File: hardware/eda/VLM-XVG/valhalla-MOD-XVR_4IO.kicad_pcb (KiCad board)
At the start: 2 copper layers, 206.2 x 99.6 mm, 126 parts, among them J1 POWER, J10 FIM_I, J11 FIM_I, J12 FIM_I, J13 FIM_I, J14 GLM_F, J15 GLM_F, J16 GLM_F, J17 GLM_F, J18 GLM_B, J19 GLM_B, J2 FIELD, J20 GLM_B, J21 GLM_B, J22 WDM_I, J23 WDM_I, J24 TM, J29 WDM_I, J3 GPIO, J31 TM_0, J32 TM_1, J34 WDM_E, J35 WDM_E, J36 WDM_E, J4 FIM_E, J5 FIM_E, J6 FIM_E, J7 FIM_E, J8 FIM_E, J9 FIM_I, Q1 IRLZ44N, Q2 IRLZ44N, Q3 2N3904, Q4 2N3904, Q5 2N3906, Q6 2N3906, U1 4N35, U2 4N35, U3 74HC14, U4 4N35, U5 4N35, U6 74HC74, U8 74HC123, U9 74HC04

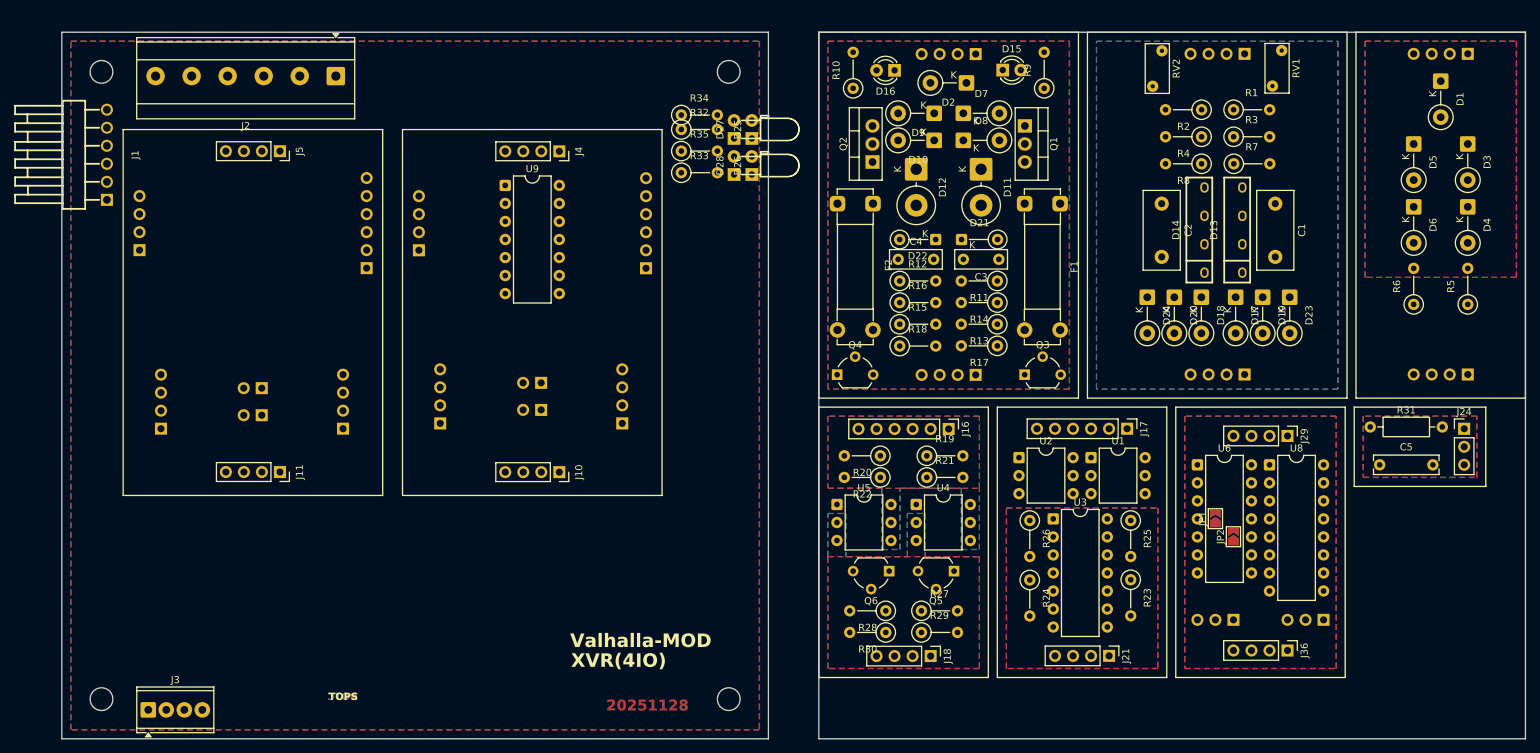
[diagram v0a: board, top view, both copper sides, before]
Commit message: UPDATE: 1st routing pass done on MOD-XVR(4IO)
 - netclass will have to be re-checked on GPI-Mains
   - clearance/creepage values between the two GPI lines
 - netclass will have to be re-checked on GPO-Power
   - ampacity of entire high-power loop
 - polarization for the field interface modules to be added
   - GPIO line modules are already polarized
   - watchdog/debouncer modules are idempotent
 - silkscreen and mechanical details are last.
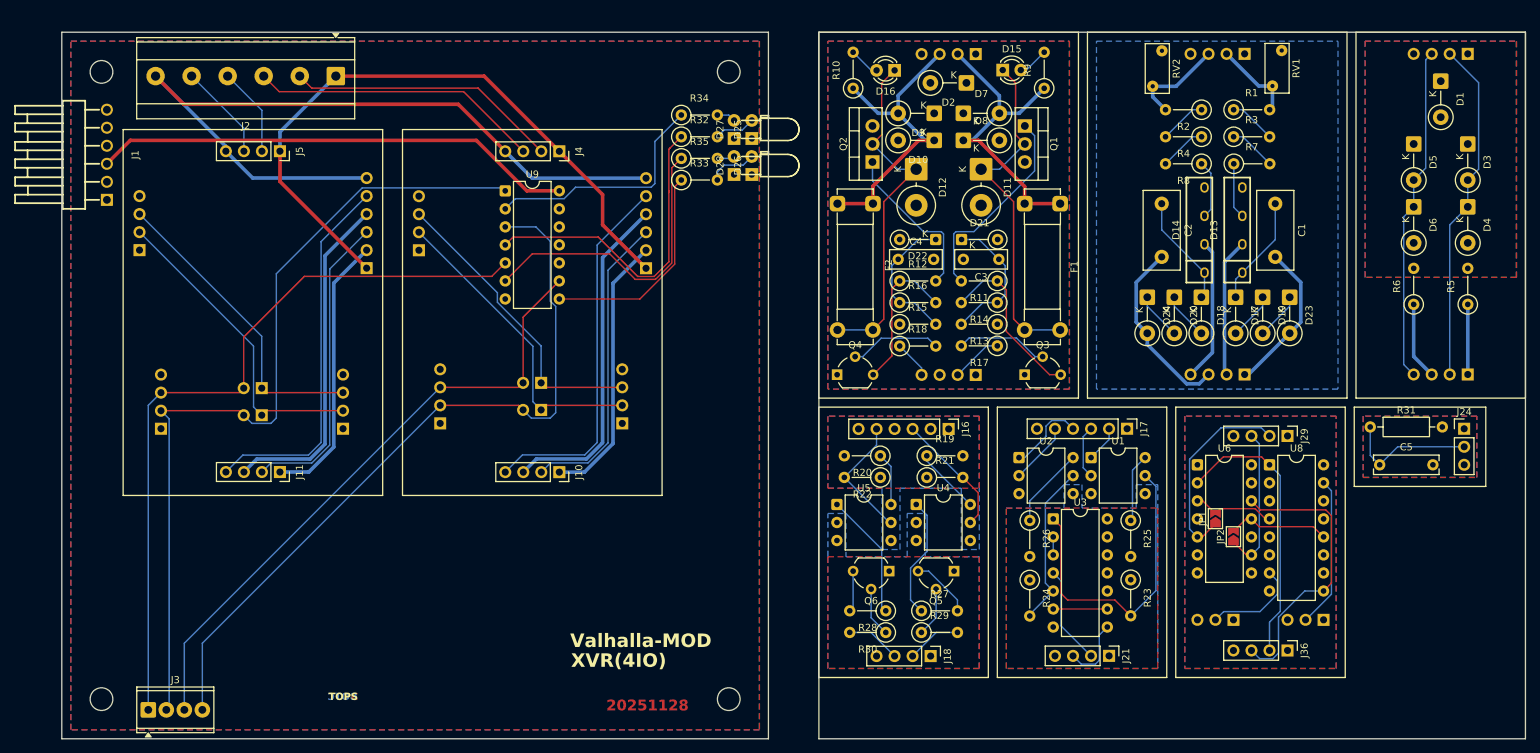
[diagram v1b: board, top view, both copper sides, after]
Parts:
- moved R32 1.03 mm to (112.7, 40.1)
- moved R33 1.03 mm to (112.7, 46.2)
- moved R35 1.03 mm to (112.7, 43.2)
- moved U9 0.76 mm to (87.9, 47.8)
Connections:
- U9 pad 1: /~{BGPIO_E_3} -> /~{BGPIO_E_2}
- U9 pad 2: Net-(R35-Pad1) -> Net-(R34-Pad1)
- U9 pad 3: /~{BGPIO_E_2} -> /~{BGPIO_E_0}
- U9 pad 4: Net-(R34-Pad1) -> Net-(R32-Pad1)
- U9 pad 5: /~{BGPIO_E_1} -> /~{BGPIO_E_3}
- U9 pad 6: Net-(R33-Pad1) -> Net-(R35-Pad1)
- U9 pad 8: Net-(R32-Pad1) -> Net-(R33-Pad1)
- U9 pad 9: /~{BGPIO_E_0} -> /~{BGPIO_E_1}
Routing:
- net /~{BGPIO_E_2}: track 0.00 -> 117.9 mm
- net /FGND: track 0.00 -> 111.2 mm
- net /~{BGPIO_E_0}: track 0.00 -> 105.8 mm
- net /~{BGPIO_E_3}: track 0.00 -> 105.8 mm
- net /FVCC: track 0.00 -> 92.8 mm
- net /~{BGPIO_E_1}: track 0.00 -> 88.8 mm
- net /LVCC: track 0.00 -> 68.1 mm
- net /~{FGPIO_I_3}: track 0.00 -> 52.5 mm
- net /~{FGPIO_I_1}: track 0.00 -> 52.3 mm
- net Net-(D11-K): track 0.00 -> 49.5 mm
- net Net-(D12-K): track 0.00 -> 49.5 mm
- net Net-(D3-A): track 0.00 -> 48.5 mm
- net /FLED_3: track 0.00 -> 47.9 mm
- net /FLED_1: track 0.00 -> 47.6 mm
- net Net-(D5-A): track 0.00 -> 47.4 mm
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
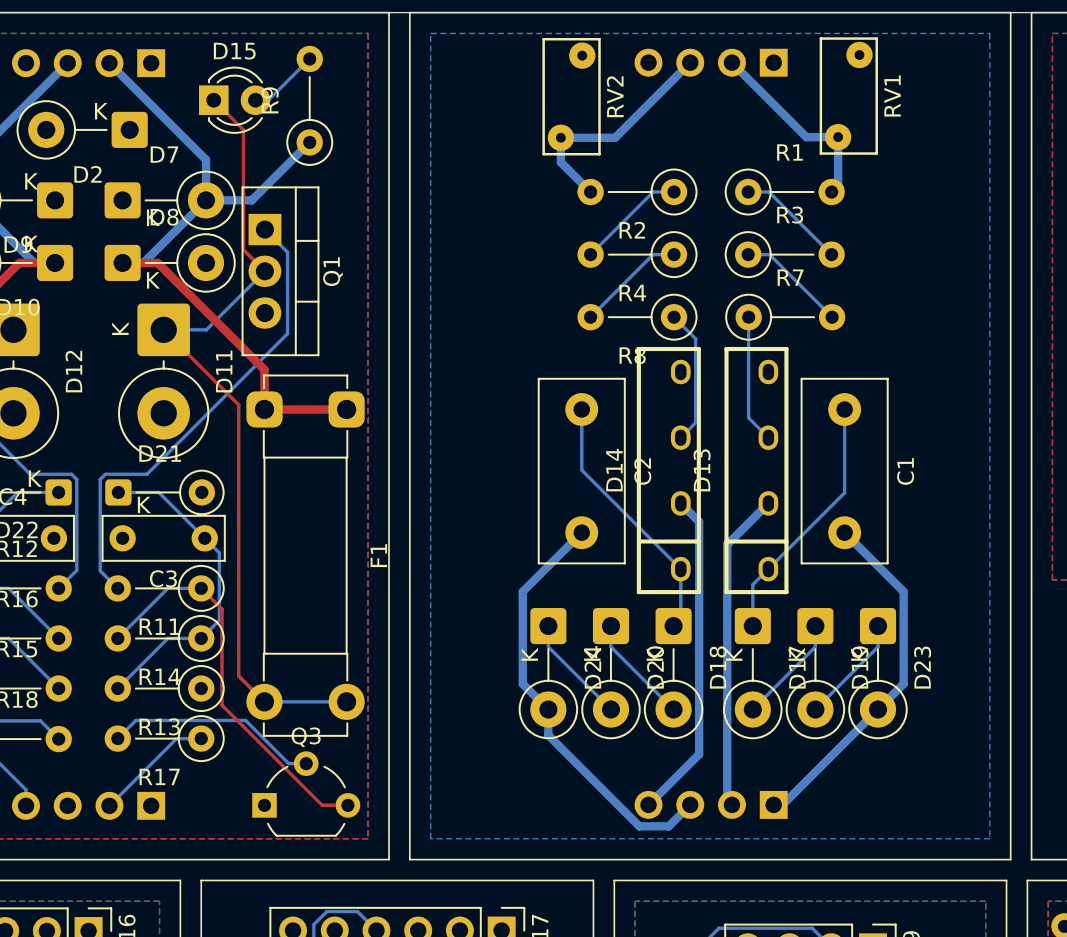
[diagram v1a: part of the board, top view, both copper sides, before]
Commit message: UPDATE: fixes for MOD-XVR(4IO)
 - fixed clearance/creepage issues on mains GPI FIM
 - fixed 1/2 of loop ampacity issues on power GPO FIM
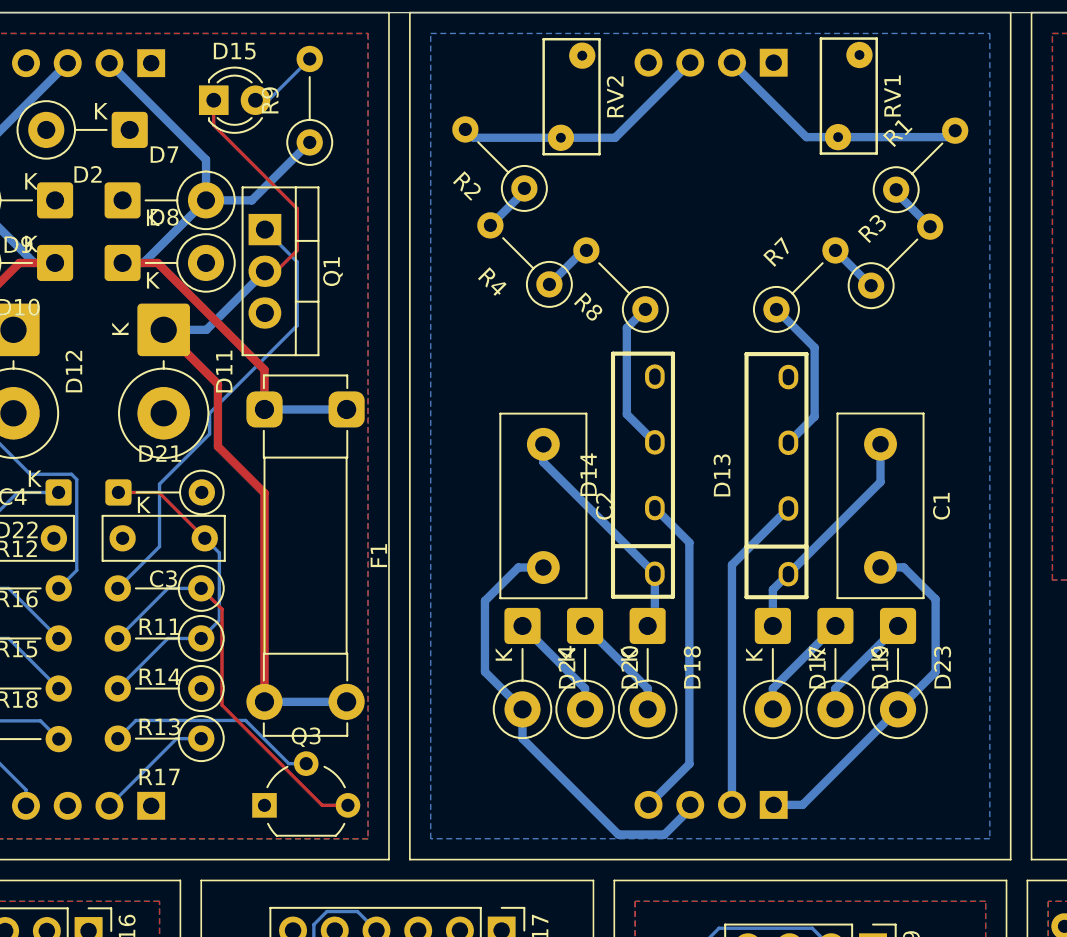
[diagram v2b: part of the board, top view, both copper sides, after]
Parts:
- moved R2 9.11 mm to (176.9, 36.1), turned to 135 degrees
- moved R1 9.01 mm to (199.5, 36.2), turned to 45 degrees
- moved R4 7.80 mm to (178.4, 41.9), turned to 135 degrees
- moved R3 7.72 mm to (198.0, 42.0), turned to 45 degrees
- moved C2 3.16 mm to (178.1, 51.7)
- moved C1 3.04 mm to (198.6, 51.7)
- moved R8 1.81 mm to (184.3, 43.5), turned to 135 degrees
- moved R7 1.76 mm to (192.2, 43.5), turned to 45 degrees
- moved D14 1.60 mm to (184.8, 53.6)
- moved D18 1.57 mm to (184.4, 62.7)
- moved D20 1.57 mm to (180.6, 62.7)
- moved D24 1.57 mm to (176.8, 62.7)
- moved D13 1.26 mm to (193.0, 53.6)
- moved D17 1.22 mm to (192.0, 62.7)
- moved D19 1.22 mm to (195.8, 62.7)
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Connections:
- U3 pad 10: unconnected-(U3-Pad10) -> /ISEC_DGND
- U3 pad 11: /ISEC_DGND -> unconnected-(U3-Pad11)
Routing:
- net Net-(J8-Pin_2): track 11.8 -> 15.6 mm
- net Net-(R3-Pad1): track 6.69 -> 3.06 mm
- net Net-(R4-Pad1): track 6.66 -> 3.11 mm
- net Net-(R1-Pad1): track 6.66 -> 3.11 mm
- net Net-(R2-Pad1): track 6.66 -> 3.11 mm
- net Net-(D11-K): track 49.5 -> 51.6 mm
- net Net-(J8-Pin_3): track 13.8 -> 15.8 mm
- net Net-(D13-Pad3): track 7.83 -> 9.74 mm
- net Net-(Q1-G): track 29.1 -> 27.2 mm
- net Net-(D14-+): track 15.9 -> 14.0 mm
- net Net-(D13-+): track 15.5 -> 13.8 mm
- net Net-(D24-A): track 25.9 -> 27.2 mm
- net Net-(D14-Pad3): track 8.26 -> 9.27 mm

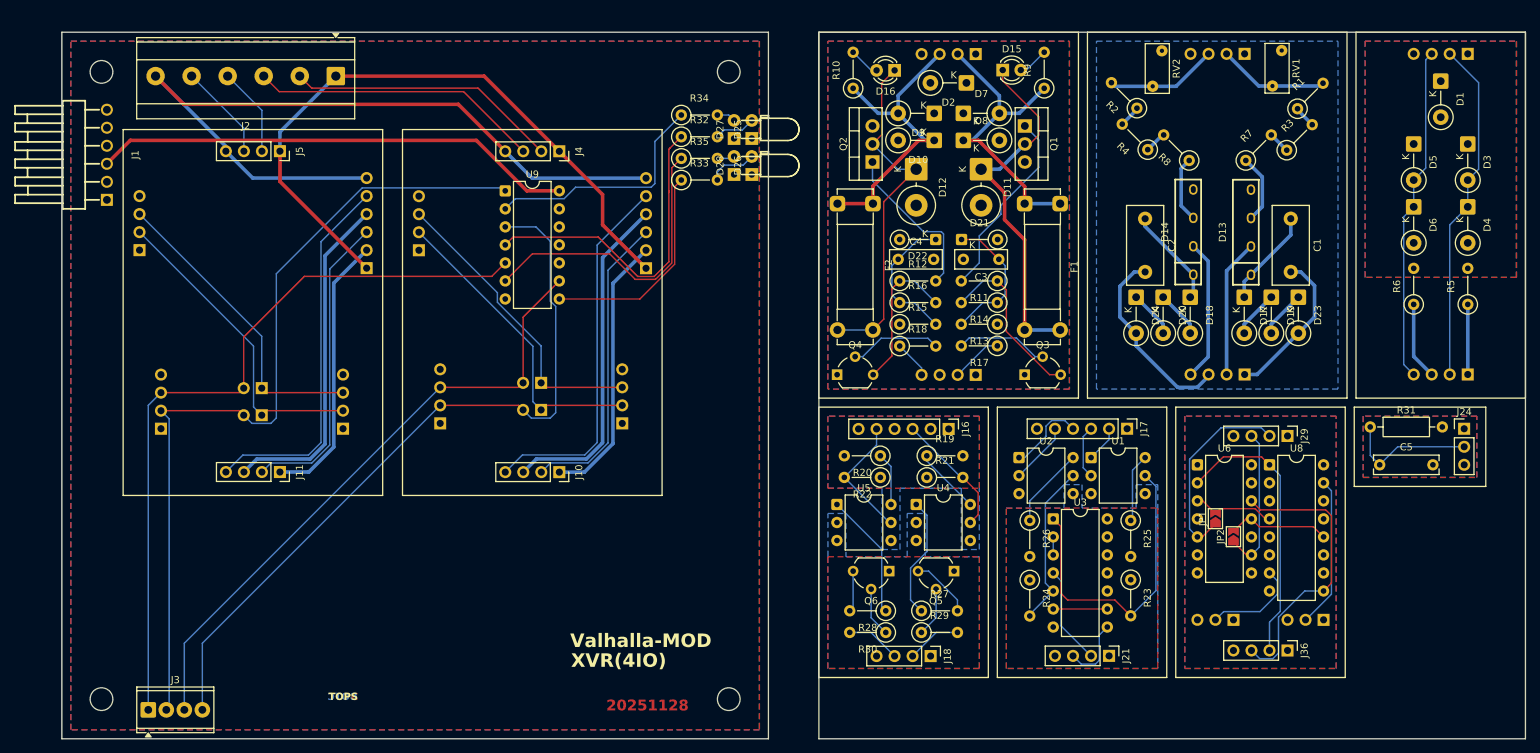
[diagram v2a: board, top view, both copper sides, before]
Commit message: UPDATE: silkscreen done on mainboard of XVR(4IO)
 - GPIO FIM mechanical polarization also done
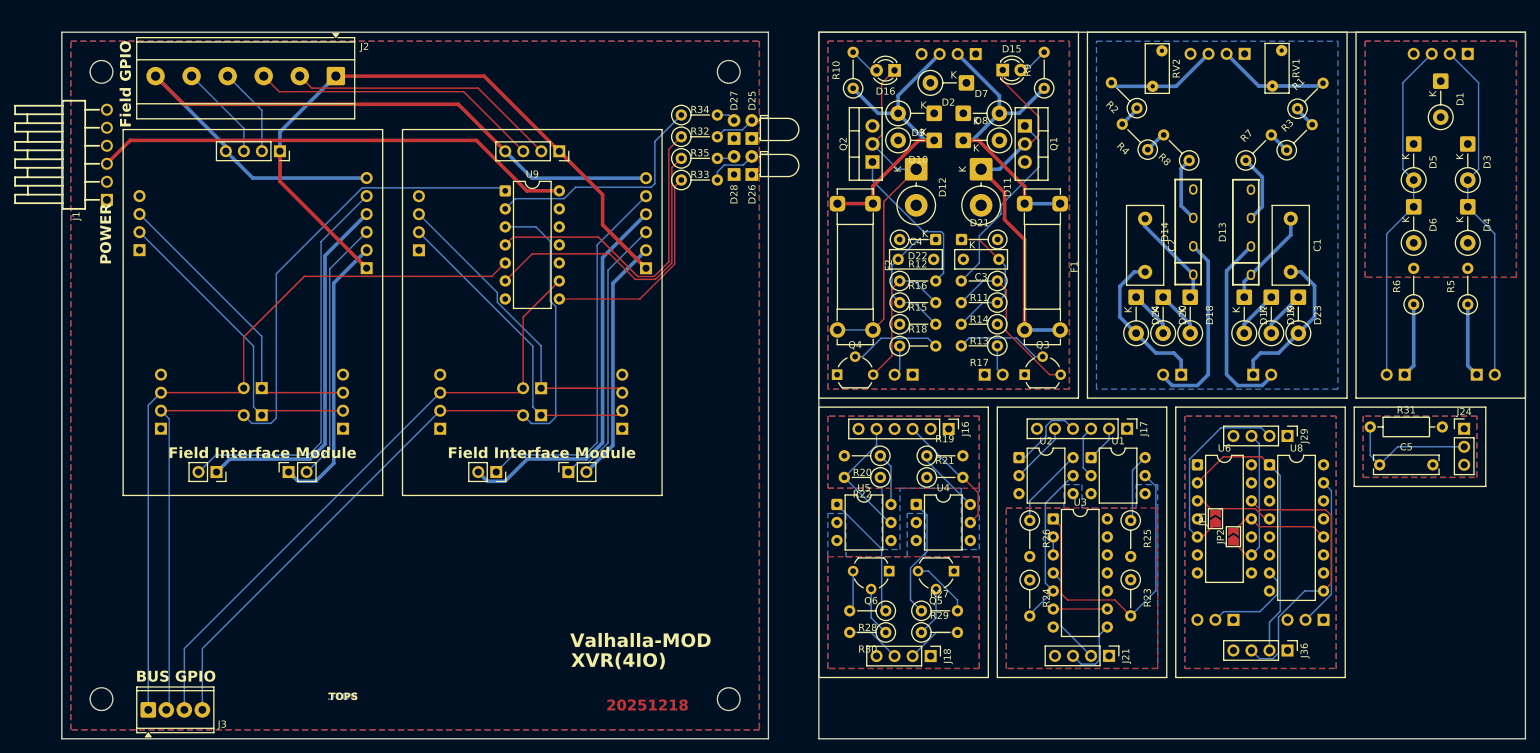
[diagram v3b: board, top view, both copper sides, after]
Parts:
- removed J10, J11: FIM_I, Connector_PinSocket_2.54mm:PinSocket_1x04_P2.54mm_Vertical
- removed J12, J13, J9: FIM_I, Connector_PinHeader_2.54mm:PinHeader_1x04_P2.54mm_Vertical
- added J25: FIM_I, Connector_PinHeader_2.54mm:PinHeader_1x02_P2.54mm_Vertical, B.Cu at (155.4, 73.7)
- added J26: FIM_I, Connector_PinHeader_2.54mm:PinHeader_1x02_P2.54mm_Vertical, B.Cu at (145.3, 73.7)
- added J27: FIM_I, Connector_PinHeader_2.54mm:PinHeader_1x02_P2.54mm_Vertical, B.Cu at (193.3, 73.7)
- added J28: FIM_I, Connector_PinHeader_2.54mm:PinHeader_1x02_P2.54mm_Vertical, B.Cu at (183.1, 73.7)
- added J30: FIM_I, Connector_PinHeader_2.54mm:PinHeader_1x02_P2.54mm_Vertical, B.Cu at (224.8, 73.7)
- added J33: FIM_I, Connector_PinHeader_2.54mm:PinHeader_1x02_P2.54mm_Vertical, B.Cu at (214.6, 73.7)
- added J37: FIM_I, Connector_PinSocket_2.54mm:PinSocket_1x02_P2.54mm_Vertical, F.Cu at (96.8, 87.4)
- added J38: FIM_I, Connector_PinSocket_2.54mm:PinSocket_1x02_P2.54mm_Vertical, F.Cu at (86.6, 87.4)
- added J39: FIM_I, Connector_PinSocket_2.54mm:PinSocket_1x02_P2.54mm_Vertical, F.Cu at (57.4, 87.4)
- added J40: FIM_I, Connector_PinSocket_2.54mm:PinSocket_1x02_P2.54mm_Vertical, F.Cu at (47.2, 87.4)
- moved J22 0.76 mm to (104.4, 81.3)
- moved J34 0.76 mm to (78.7, 81.3)
- moved JP5 0.76 mm to (92.9, 75.6)
- moved JP3 0.76 mm to (92.9, 79.4)
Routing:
- net Net-(D13--): track 19.5 -> 27.2 mm
- net /FLED_1: track 47.6 -> 55.1 mm
- net Net-(D14--): track 20.0 -> 26.7 mm
- net /~{FGPIO_I_2}: track 43.3 -> 37.3 mm
- net Net-(D24-A): track 27.2 -> 21.9 mm
- net /~{FGPIO_I_3}: track 52.5 -> 56.4 mm
- net /FLED_3: track 47.9 -> 51.8 mm
- net /~{FGPIO_I_0}: track 43.0 -> 39.2 mm
- net /FLED_0: track 38.4 -> 34.7 mm
- net Net-(J25-Pin_2): track 7.28 -> 4.38 mm
- net Net-(D5-A): track 47.4 -> 49.1 mm
- net /~{FGPIO_I_1}: track 52.3 -> 53.5 mm
- net /FLED_2: track 38.7 -> 39.9 mm
- net Net-(J26-Pin_2): track 5.34 -> 4.33 mm
- net /~{BGPIO_I_1}: track 42.6 -> 43.4 mm
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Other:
- board text added: "20251218"
- board text added: "BUS"
- board text added: "BUS GPIO"
- board text added: "Field"
- board text added: "Field GPIO"
- board text added: "Field Interface Module"
- board text added: "GPIO"
- board text added: "GPIO Line Module"
- board text added: "Line"
- board text added: "Module"
- board text added: "POWER"
- board text added: "Watchdog/Debouncer Module"
- board text added: "~{WD/DB}"
- board text removed: "20251128"
